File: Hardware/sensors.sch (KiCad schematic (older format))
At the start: 2 parts, among them U3 LM75CIMM-3

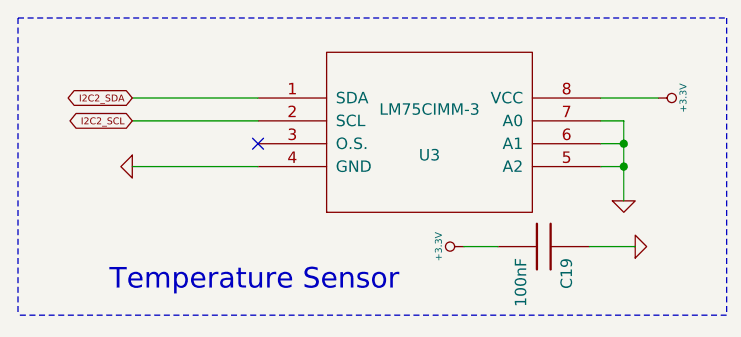
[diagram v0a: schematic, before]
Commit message: Created PCB for new version with parallel display & sram
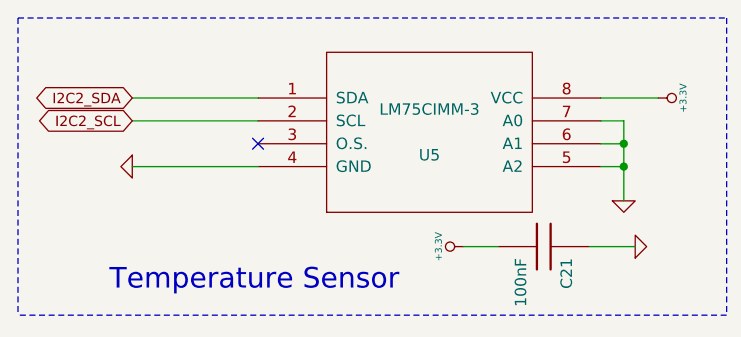
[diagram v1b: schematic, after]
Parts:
- renumbered C19 to C21, U3 to U5
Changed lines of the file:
@@
-EESchema Schematic File Version 2  date 20.09.2010 21:14:13
+EESchema Schematic File Version 2  date Fr 24 Sep 2010 05:02:11 CEST
 LIBS:power
 LIBS:device
@@
 LIBS:valves
 LIBS:STM32F10xZx
-LIBS:farnell
 LIBS:welectronic
 LIBS:LM75CIM
 LIBS:AS7C34098A
+LIBS:CONN_17x2
+LIBS:LM3940
 LIBS:mainboard-cache
 EELAYER 24  0
@@
 Sheet 2 4
 Title ""
-Date "20 sep 2010"
+Date "24 sep 2010"
 Rev ""
 Comp ""
@@
 	2450 1500 2600 1500
 $Comp
-L +3.3V #PWR037
+L +3.3V #PWR039
 U 1 1 4C96A16E
 P 2450 1500
-F 0 "#PWR037" H 2450 1460 30  0001 C CNN
+F 0 "#PWR039" H 2450 1460 30  0001 C CNN
 F 1 "+3.3V" H 2450 1610 30  0000 C CNN
 	1    2450 1500
@@
 $EndComp
 $Comp
-L GND #PWR038
+L GND #PWR040
 U 1 1 4C96A16A
 P 3200 1500
-F 0 "#PWR038" H 3200 1500 30  0001 C CNN
+F 0 "#PWR040" H 3200 1500 30  0001 C CNN
 F 1 "GND" H 3200 1430 30  0001 C CNN
 	1    3200 1500
@@
 $EndComp
 $Comp
-L C C19
+L C C21
 U 1 1 4C96A165
 P 2800 1500
-F 0 "C19" H 2850 1600 50  0000 L CNN
+F 0 "C21" H 2850 1600 50  0000 L CNN
 F 1 "100nF" H 2850 1400 50  0000 L CNN
 	1    2800 1500
@@
 Temperature Sensor
 $Comp
-L +3.3V #PWR039
+L +3.3V #PWR041
 U 1 1 4C969FB2
 P 3300 850
-F 0 "#PWR039" H 3300 810 30  0001 C CNN
+F 0 "#PWR041" H 3300 810 30  0001 C CNN
 F 1 "+3.3V" H 3300 960 30  0000 C CNN
 	1    3300 850
@@
 $EndComp
 $Comp
-L GND #PWR040
+L GND #PWR042
 U 1 1 4C969FAE
 P 3150 1300
-F 0 "#PWR040" H 3150 1300 30  0001 C CNN
+F 0 "#PWR042" H 3150 1300 30  0001 C CNN
 F 1 "GND" H 3150 1230 30  0001 C CNN
 	1    3150 1300
@@
 $EndComp
 $Comp
-L GND #PWR041
+L GND #PWR043
 U 1 1 4C969FA8
 P 1000 1150
-F 0 "#PWR041" H 1000 1150 30  0001 C CNN
+F 0 "#PWR043" H 1000 1150 30  0001 C CNN
 F 1 "GND" H 1000 1080 30  0001 C CNN
 	1    1000 1150
@@
 $EndComp
 NoConn ~ 1550 1050
-Text GLabel 1000 950  0    30   BiDi ~ 0
+Text GLabel 1000 950  0    45   BiDi ~ 0
 I2C2_SCL
-Text GLabel 1000 850  0    30   BiDi ~ 0
+Text GLabel 1000 850  0    45   BiDi ~ 0
 I2C2_SDA
 $Comp
-L LM75CIM U3
+L LM75CIM U5
 U 1 1 4C969F76
 P 2300 1000
-F 0 "U3" H 2300 900 50  0000 C CNN
+F 0 "U5" H 2300 900 50  0000 C CNN
 F 1 "LM75CIMM-3" H 2300 1100 50  0000 C CNN
 	1    2300 1000

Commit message: new version schematics
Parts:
- removed C21: 100nF, symbol C
- removed U5: LM75CIMM-3, symbol LM75CIM
- added C701: 0.3uF, symbol C
- added C702, C703, C704, C705, C706, C707: 100nF, symbol C
- added P701: Sensors, symbol CONN_8
- added R701, R709, R711, R712, R713, R714, R715: 10k, symbol R
- added R702, R716, R717: 4k7, symbol R
- added R703, R704, R705, R706, R707, R708: 2k7, symbol R
- added R710: 120, symbol R
- added U701, U702, U703, U704, U705, U706, U707: BAS40-04, symbol BAS40-04
- added U708, U709: DS18B20, symbol DS1820
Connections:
- net +3.3V: now also R701.2, R716.1, R717.1, U701.2, U702.2, U703.2, U708.3 (VCC), U709.3 (VCC)
- net GND: now also C701.1, C702.1, C703.1, R702.1, R703.1, R704.1, U701.1, U702.1, U703.1, U708.1 (GND), U709.1 (GND)
- new net: P701.1 (P1), R709.1
- new net: P701.5 (P5), R712.1
- new net: P701.6 (P6), R713.1
- new net: P701.7 (P7), R714.1
- new net: P701.8 (P8), R715.1
- new net: P701.3 (P3), R711.1
- new net: P701.2 (P2), R710.1
- new net +12V: P701.4 (P4)
- new net CoolantTemp: C706.2, R707.2, R714.2, U706.3
- new net FuelLevel: C705.2, R706.2, R713.2, U705.3
- new net GNDA: C704.1, C705.1, C706.1, C707.1, R705.1, R706.1, R707.1, R708.1, U704.1, U705.1, U706.1, U707.1
- new net RPM: C704.2, R705.2, R712.2, U704.3
- new net ReserveSensor: C707.2, R708.2, R715.2, U707.3
- new net Speed-Reed: C703.2, R702.2, R704.2, R711.2, U703.3
- new net TEMP1: R716.2, U708.2 (DQ)
- new net TEMP2: R717.2, U709.2 (DQ)
- new net VAA: U704.2, U705.2, U706.2, U707.2
- new net ~FuelConsumption: C702.2, R701.1, R710.2, U701.3
- new net ~FuelPump: C701.2, R703.2, R709.2, U702.3
- no-connect marks 1 -> 0
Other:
- note added: "(8 Signals/rev?)"
- note added: "(Analog)"
- note added: "(Low when active)"
- note added: "(OpenCollector)"
- note added: "http://www.mikrocontroller.net/articles/Temperatursensor"
- note removed: "Temperature Sensor"
